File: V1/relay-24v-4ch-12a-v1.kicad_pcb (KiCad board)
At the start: 2 copper layers, 53 x 67.8 mm, 24 parts, among them J1 DB141V-2.54-2P, J2 DB141V-2.54-4P, J3 DB142V-5.08-4P, J4 DB142V-5.08-4P, K1 G5PZ-1A, K2 G5PZ-1A, K3 G5PZ-1A, K4 G5PZ-1A

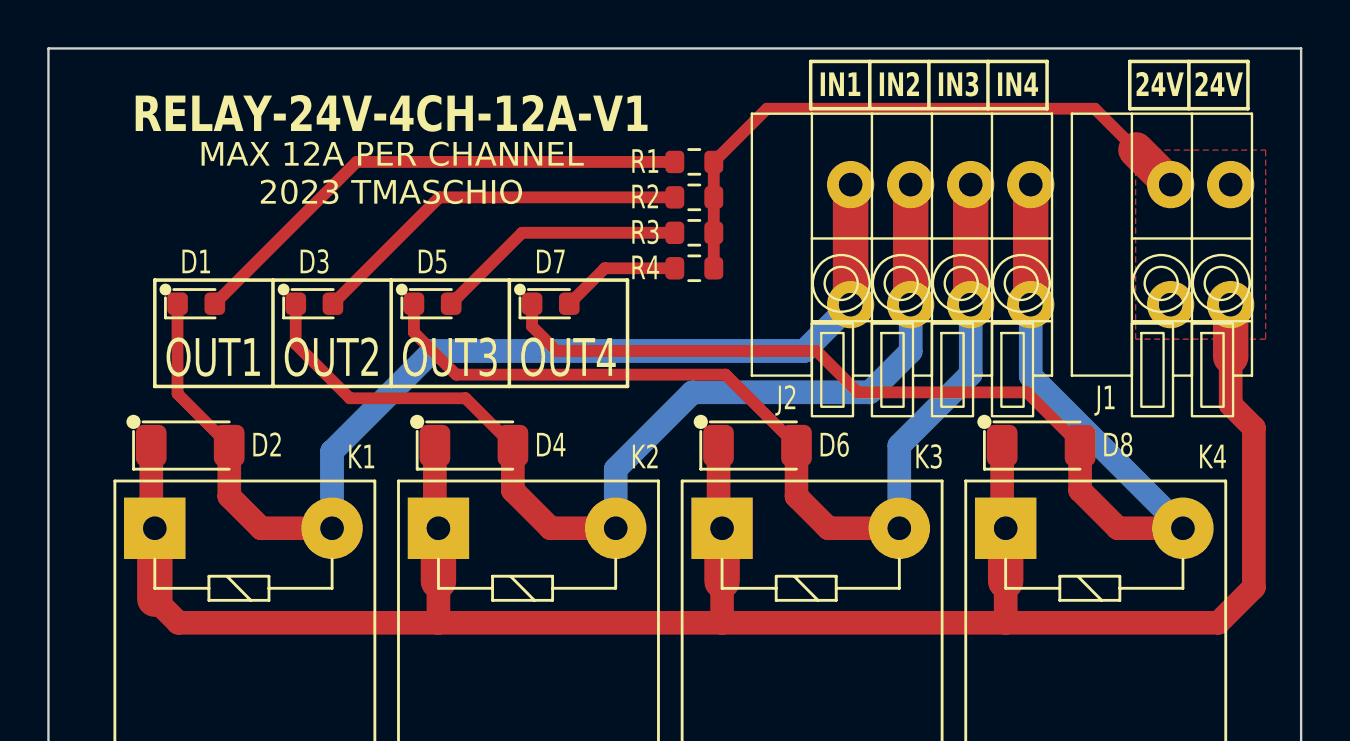
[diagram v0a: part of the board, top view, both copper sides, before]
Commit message: Replaced terminal block
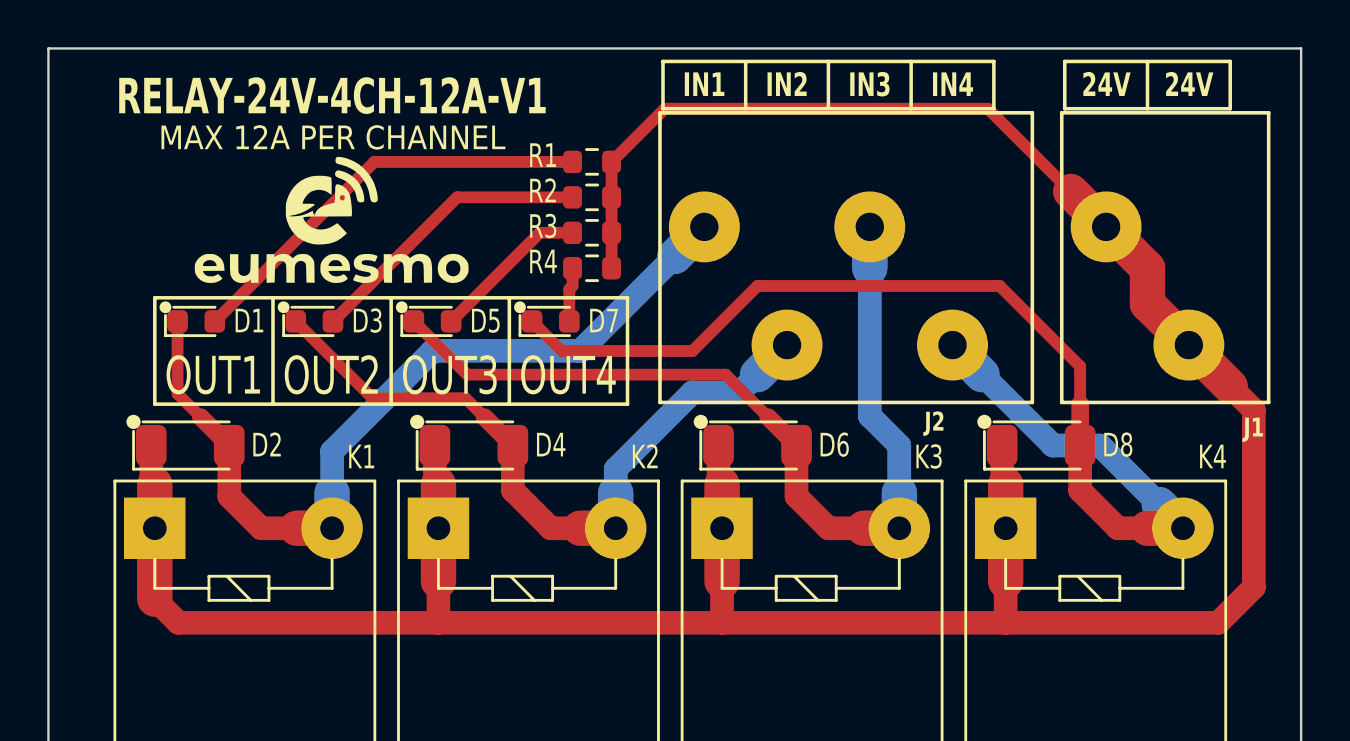
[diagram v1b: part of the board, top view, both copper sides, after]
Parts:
- added G***: LOGO, Tales:Eumesmo_small_silk, F.Cu at (137.0, 69.5)
- J1: value DB141V-2.54-2P -> +24V; footprint Tales:TerminalBlock_Dibo_DB141V-2.54-2P_1x02_P2.54mm_Vertical -> Tales:TerminalBlock_Wago_250-202_1x02_P3.5mm_45Degree
- J2: value DB141V-2.54-4P -> INPUTS; footprint Tales:TerminalBlock_Dibo_DB141V-2.54-4P_1x04_P2.54mm_Vertical -> Tales:TerminalBlock_Wago_250-204_1x04_P3.5mm_45Degree
- moved J2 5.06 mm to (158.0, 72.2)
- moved R1 4.32 mm to (148.0, 67.0)
- moved R2 4.32 mm to (148.0, 68.5)
- moved R3 4.32 mm to (148.0, 70.0)
- moved R4 4.32 mm to (148.0, 71.5)
- moved J1 2.85 mm to (171.5, 72.2)
- moved D1 0.75 mm to (131.2, 73.8)
- moved D3 0.75 mm to (136.2, 73.8)
- moved D5 0.75 mm to (141.2, 73.8)
- moved D7 0.75 mm to (146.2, 73.8)
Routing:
- net /IN2: track 43.7 -> 30.2 mm
- net /IN1: track 46.8 -> 36.2 mm
- net +24V: track 115.2 -> 123.1 mm
- net /LED2: track 16.3 -> 12.3 mm
- net /LED1: track 21.9 -> 17.9 mm
- net /LED3: track 10.7 -> 6.69 mm
- net /IN3: track 42.2 -> 38.7 mm
- net /LED4: track 5.08 -> 2.31 mm
- net /IN4: track 50.4 -> 49.5 mm
- removed copper zone on F.Cu, net +24V
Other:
- board text added: "MAX 12A PER CHANNEL"
- board text removed: "MAX 12A PER CHANNEL 2023 TMASCHIO"

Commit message: Silkscreen updated
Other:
- board text added: "RELAY-24V-4CH-12A-V1.1"
- board text removed: "RELAY-24V-4CH-12A-V1"
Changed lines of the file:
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@@
 		)
 	)
-	(gr_text "RELAY-24V-4CH-12A-V1"
+	(gr_text "RELAY-24V-4CH-12A-V1.1"
 		(at 137 64.25 0)
 		(layer "F.SilkS")

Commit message: Replaced input terminal blocks for 3.5mm pitch.
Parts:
- J1: value +24V -> 250-202
- J2: value INPUTS -> 250-204
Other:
- board text added: "RELAY-24V-4CH-12A-V1"
- board text added: "V1.1 2026-06-02"
- board text removed: "RELAY-24V-4CH-12A-V1.1"
